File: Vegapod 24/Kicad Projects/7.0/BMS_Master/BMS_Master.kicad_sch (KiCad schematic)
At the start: 87 parts, among them IC1 B0505S-2W, J1 LV Battery, J2 ST-Link, J3 Conn_01x06_Pin, K1 ECK200BHAAEA, K2 ECK200BHAAEA, Q1 SI2318CDS (SI2318), Q2 SI2318CDS (SI2318), U1 KA78M12_TO252, U11 LM324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

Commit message: BMS Master completed
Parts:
- added C33: 100n, Capacitor_SMD:C_0805_2012Metric_Pad1.18x1.45mm_HandSolder, symbol Device:C_Small
- added C34, C35: 10uF, Capacitor_SMD:C_1206_3216Metric_Pad1.33x1.80mm_HandSolder, symbol Device:C_Small
- added J4: Batt Comm, Connector_PinSocket_2.00mm:PinSocket_1x05_P2.00mm_Vertical, symbol Connector:Conn_01x05_Pin
- added R32, R33, R34, R35, R36, R37: 470, Resistor_SMD:R_0805_2012Metric_Pad1.20x1.40mm_HandSolder, symbol Device:R_Small
- added U10, U14: 6N137, Package_SO:SSO-8_6.7x9.8mm_P2.54mm_Clearance8mm, symbol Isolator:6N137
- added U15: B0505S-1WR3, B0505S_MNS, symbol B0505-1WR3:B0505S-1WR3
- added U16: EL814, Package_DIP:SMDIP-4_W9.53mm_Clearance8mm, symbol Isolator:EL814
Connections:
- net +5VD: now also C33.2, C34.1, R34.2, U14.7 (EN), U14.8 (VCC), U15.2 (VIN)
- net GNDD: now also C33.1, C34.2, U10.3 (C), U14.5 (GND), U15.1 (GND), U16.2
- net RX: now also R34.1, U14.6 (VO)
- net TX: now also R33.2
- net PA8: now reaches U13.42 (PA8)
- net PA8: now also R37.2
- new net: J4.4 (Pin_4), R32.1, U10.6 (VO)
- new net: C35.1, J4.2 (Pin_2), R32.2, U10.7 (EN), U10.8 (VCC), U15.4 (+VO), U16.4
- new net: J4.5 (Pin_5), R36.1, U16.3
- new net: J4.3 (Pin_3), R35.1
- new net: R35.2, U14.2 (A)
- new net: R33.1, U10.2 (A)
- new net: R37.1, U16.1
- new net GND1: C35.2, J4.1 (Pin_1), R36.2, U10.5 (GND), U14.3 (C), U15.3 (0V)

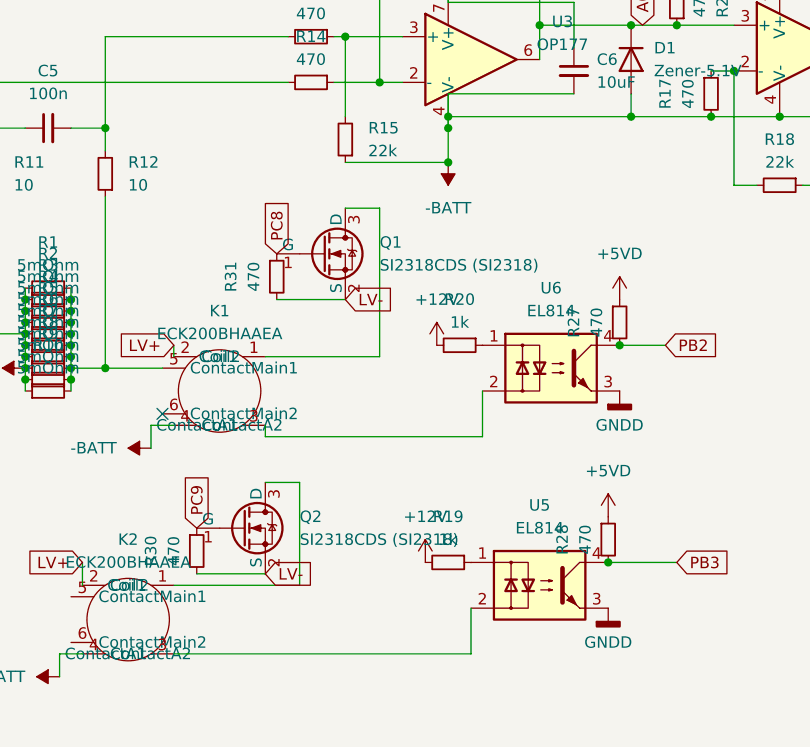
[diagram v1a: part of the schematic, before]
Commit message: Flyback diode for contactor
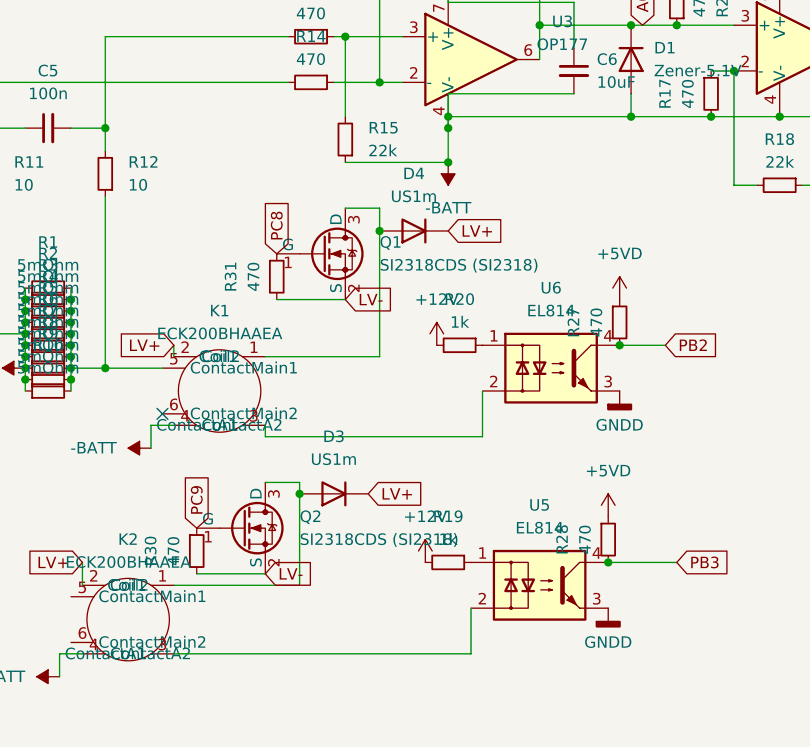
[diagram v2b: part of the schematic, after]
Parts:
- added D3, D4: US1m, Diode_SMD:D_SMA-SMB_Universal_Handsoldering, symbol Device:D
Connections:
- net LV+: now also D3.1 (K), D4.1 (K)
- net at K1.1 (Coil1), Q1.3 (D): now also D4.2 (A)
- net at K2.1 (Coil1), Q2.3 (D): now also D3.2 (A)
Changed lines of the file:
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@@
   (junction (at 214.63 86.36) (diameter 0) (color 0 0 0 0)
   )
+  (junction (at 78.74 111.76) (diameter 0) (color 0 0 0 0)
+  )
   (junction (at 482.6 78.74) (diameter 0) (color 0 0 0 0)
   )
@@
   (junction (at 50.8 50.8) (diameter 0) (color 0 0 0 0)
   )
+  (junction (at 87.63 82.55) (diameter 0) (color 0 0 0 0)
+  )
   (no_connect (at 63.5 102.87))
   (wire (pts (xy 367.03 52.07) (xy 358.14 52.07))
@@
     (stroke (width 0) (type default))
   )
-  (wire (pts (xy 87.63 80.01) (xy 87.63 96.52))
+  (wire (pts (xy 87.63 80.01) (xy 87.63 82.55))
     (stroke (width 0) (type default))
   )
@@
     (stroke (width 0) (type default))
   )
-  (wire (pts (xy 78.74 110.49) (xy 78.74 121.92))
+  (wire (pts (xy 78.74 110.49) (xy 78.74 111.76))
     (stroke (width 0) (type default))
   )
@@
     (stroke (width 0) (type default))
   )
+  (wire (pts (xy 78.74 111.76) (xy 78.74 121.92))
+    (stroke (width 0) (type default))
+  )
   (wire (pts (xy 245.11 92.71) (xy 260.35 92.71))
     (stroke (width 0) (type default))
@@
     (stroke (width 0) (type default))
   )
+  (wire (pts (xy 87.63 82.55) (xy 87.63 96.52))
+    (stroke (width 0) (type default))
+  )
   (wire (pts (xy 146.05 69.85) (xy 132.08 69.85))
     (stroke (width 0) (type default))
@@
     )
   )
+  (global_label "LV+" (shape input) (at 95.25 82.55 0) (fields_autoplaced)
+    (effects (font (size 1.27 1.27)) (justify left))
+    (property "Intersheetrefs" "${INTERSHEET_REFS}" (at 101.9243 82.55 0)
+      (effects (font (size 1.27 1.27)) (justify left) hide)
+    )
+  )
   (global_label "TX" (shape input) (at 358.14 90.17 180) (fields_autoplaced)
     (effects (font (size 1.27 1.27)) (justify right))
@@
     )
   )
+  (global_label "LV+" (shape input) (at 86.36 111.76 0) (fields_autoplaced)
+    (effects (font (size 1.27 1.27)) (justify left))
+    (property "Intersheetrefs" "${INTERSHEET_REFS}" (at 93.0343 111.76 0)
+      (effects (font (size 1.27 1.27)) (justify left) hide)
+    )
+  )
   (global_label "SWDIO" (shape input) (at 427.99 27.94 270) (fields_autoplaced)
     (effects (font (size 1.27 1.27)) (justify right))
@@
     )
   )
+  (symbol (lib_id "Device:D") (at 91.44 82.55 180) (unit 1)
+    (in_bom yes) (on_board yes) (dnp no) (fields_autoplaced)
+    (property "Reference" "D4" (at 91.44 76.2 0)
+      (effects (font (size 1.27 1.27)))
+    )
+    (property "Value" "US1m" (at 91.44 78.74 0)
+      (effects (font (size 1.27 1.27)))
+    )
+    (property "Footprint" "Diode_SMD:D_SMA-SMB_Universal_Handsoldering" (at 91.44 82.55 0)
+      (effects (font (size 1.27 1.27)) hide)
+    )
+    (property "Datasheet" "~" (at 91.44 82.55 0)
+      (effects (font (size 1.27 1.27)) hide)
+    )
+    (property "Sim.Device" "D" (at 91.44 82.55 0)
+      (effects (font (size 1.27 1.27)) hide)
+    )
+    (property "Sim.Pins" "1=K 2=A" (at 91.44 82.55 0)
+      (effects (font (size 1.27 1.27)) hide)
+    )
+    (pin "2")
+    (pin "1")
+    (instances
+      (project "BMS_Master"
+        (path "/932638ee-bc30-42e0-97cd-e4762c194981"
+          (reference "D4") (unit 1)
+        )
+      )
+    )
+  )
   (symbol (lib_id "Device:C_Small") (at 58.42 48.26 0) (unit 1)
     (in_bom yes) (on_board yes) (dnp no) (fields_autoplaced)
@@
         )
       )
+    )
+  )
+  (symbol (lib_id "Device:D") (at 82.55 111.76 180) (unit 1)
+    (in_bom yes) (on_board yes) (dnp no) (fields_autoplaced)
+    (property "Reference" "D3" (at 82.55 105.41 0)
+      (effects (font (size 1.27 1.27)))
+    )
+    (property "Value" "US1m" (at 82.55 107.95 0)
+      (effects (font (size 1.27 1.27)))
+    )
+    (property "Footprint" "Diode_SMD:D_SMA-SMB_Universal_Handsoldering" (at 82.55 111.76 0)
+      (effects (font (size 1.27 1.27)) hide)
+    )
+    (property "Datasheet" "~" (at 82.55 111.76 0)
+      (effects (font (size 1.27 1.27)) hide)
+    )
+    (property "Sim.Device" "D" (at 82.55 111.76 0)
+      (effects (font (size 1.27 1.27)) hide)
+    )
+    (property "Sim.Pins" "1=K 2=A" (at 82.55 111.76 0)
+      (effects (font (size 1.27 1.27)) hide)
+    )
+    (pin "2")
+    (pin "1")
+    (instances
+      (project "BMS_Master"
+        (path "/932638ee-bc30-42e0-97cd-e4762c194981"
+          (reference "D3") (unit 1)
+        )
+      )

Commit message: Add boot pin conn. (forgor💀)
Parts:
- added R59: SHORT OUT, Resistor_SMD:R_0402_1005Metric, symbol Device:R
- added R60: Open Circuit, Resistor_SMD:R_0402_1005Metric, symbol Device:R
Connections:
- net +3.3V: now also R60.2
- net GNDD: now also R59.1
- net at U13.61 (PB8): now also R59.2, R60.1
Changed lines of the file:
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@@
   (junction (at 102.87 22.86) (diameter 0) (color 0 0 0 0)
   )
+  (junction (at 405.13 120.65) (diameter 0) (color 0 0 0 0)
+  )
   (junction (at 53.34 91.44) (diameter 0) (color 0 0 0 0)
   )
@@
     (stroke (width 0) (type default))
   )
+  (wire (pts (xy 393.7 120.65) (xy 405.13 120.65))
+    (stroke (width 0) (type default))
+  )
   (wire (pts (xy 149.86 60.96) (xy 149.86 55.88))
     (stroke (width 0) (type default))
@@
     )
   )
+  (symbol (lib_id "power:GNDD") (at 405.13 128.27 0) (unit 1)
+    (in_bom yes) (on_board yes) (dnp no) (fields_autoplaced)
+    (property "Reference" "#PWR060" (at 405.13 134.62 0)
+      (effects (font (size 1.27 1.27)) hide)
+    )
+    (property "Value" "GNDD" (at 405.13 132.08 0)
+      (effects (font (size 1.27 1.27)))
+    )
+    (property "Footprint" "" (at 405.13 128.27 0)
+      (effects (font (size 1.27 1.27)) hide)
+    )
+    (property "Datasheet" "" (at 405.13 128.27 0)
+      (effects (font (size 1.27 1.27)) hide)
+    )
+    (pin "1")
+    (instances
+      (project "BMS_Master"
+        (path "/932638ee-bc30-42e0-97cd-e4762c194981"
+          (reference "#PWR060") (unit 1)
+        )
+      )
+    )
+  )
   (symbol (lib_id "power:+12V") (at 95.25 55.88 0) (unit 1)
     (in_bom yes) (on_board yes) (dnp no) (fields_autoplaced)
@@
     )
   )
+  (symbol (lib_id "Device:R") (at 405.13 116.84 180) (unit 1)
+    (in_bom yes) (on_board yes) (dnp no) (fields_autoplaced)
+    (property "Reference" "R60" (at 407.67 115.57 0)
+      (effects (font (size 1.27 1.27)) (justify right))
+    )
+    (property "Value" "Open Circuit" (at 407.67 118.11 0)
+      (effects (font (size 1.27 1.27)) (justify right))
+    )
+    (property "Footprint" "Resistor_SMD:R_0402_1005Metric" (at 406.908 116.84 90)
+      (effects (font (size 1.27 1.27)) hide)
+    )
+    (property "Datasheet" "~" (at 405.13 116.84 0)
+      (effects (font (size 1.27 1.27)) hide)
+    )
+    (pin "2")
+    (pin "1")
+    (instances
+      (project "LU"
+        (path "/735d61e3-154f-498a-961e-67a9bf0dff66"
+          (reference "R60") (unit 1)
+        )
+      )
+      (project "BMS_Master"
+        (path "/932638ee-bc30-42e0-97cd-e4762c194981"
+          (reference "R38") (unit 1)
+        )
+      )
+    )
+  )
   (symbol (lib_id "Device:C_Small") (at 135.89 33.02 0) (unit 1)
     (in_bom yes) (on_board yes) (dnp no) (fields_autoplaced)
@@
     )
   )
+  (symbol (lib_id "Device:R") (at 405.13 124.46 180) (unit 1)
+    (in_bom yes) (on_board yes) (dnp no) (fields_autoplaced)
+    (property "Reference" "R59" (at 407.67 123.19 0)
+      (effects (font (size 1.27 1.27)) (justify right))
+    )
+    (property "Value" "SHORT OUT" (at 407.67 125.73 0)
+      (effects (font (size 1.27 1.27)) (justify right))
+    )
+    (property "Footprint" "Resistor_SMD:R_0402_1005Metric" (at 406.908 124.46 90)
+      (effects (font (size 1.27 1.27)) hide)
+    )
+    (property "Datasheet" "~" (at 405.13 124.46 0)
+      (effects (font (size 1.27 1.27)) hide)
+    )
+    (pin "2")
+    (pin "1")
+    (instances
+      (project "LU"
+        (path "/735d61e3-154f-498a-961e-67a9bf0dff66"
+          (reference "R59") (unit 1)
+        )
+      )
+      (project "BMS_Master"
+        (path "/932638ee-bc30-42e0-97cd-e4762c194981"
+          (reference "R39") (unit 1)
+        )
+      )
+    )
+  )
   (symbol (lib_id "power:+3.3V") (at 186.69 20.32 0) (unit 1)
     (in_bom yes) (on_board yes) (dnp no) (fields_autoplaced)
@@
         )
       )
+    )
+  )
+  (symbol (lib_id "power:+3.3V") (at 405.13 113.03 0) (unit 1)
+    (in_bom yes) (on_board yes) (dnp no) (fields_autoplaced)
+    (property "Reference" "#PWR061" (at 405.13 116.84 0)
+      (effects (font (size 1.27 1.27)) hide)
+    )
+    (property "Value" "+3.3V" (at 405.13 107.95 0)
+      (effects (font (size 1.27 1.27)))
+    )
+    (property "Footprint" "" (at 405.13 113.03 0)
+      (effects (font (size 1.27 1.27)) hide)
+    )
+    (property "Datasheet" "" (at 405.13 113.03 0)
+      (effects (font (size 1.27 1.27)) hide)
+    )
+    (pin "1")
+    (instances
+      (project "BMS_Master"
+        (path "/932638ee-bc30-42e0-97cd-e4762c194981"
+          (reference "#PWR061") (unit 1)
+        )
+      )

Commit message: BMS Master changes because fucked up
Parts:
- added C36, C37: 10uF, Capacitor_SMD:C_1206_3216Metric_Pad1.33x1.80mm_HandSolder, symbol Device:C_Small
- added U17: B0505S-1WR3, B0505S_MNS, symbol B0505-1WR3:B0505S-1WR3
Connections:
- net +5V: now also C36.2, U17.2 (VIN)
- net -BATT: now also C36.1, C37.1, U17.1 (GND), U17.4 (+VO); no longer C11.2, C6.2, U3.4 (V-), U4.4 (V-)
- new net -5V: C11.2, C37.2, C6.2, U17.3 (0V), U3.4 (V-), U4.4 (V-)
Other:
- moved on the sheet: D2

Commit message: BMS Master final changes
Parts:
- added Q1 (x2): IRLZ44N, Package_TO_SOT_THT:TO-220-3_Vertical, symbol Transistor_FET:IRLZ44N
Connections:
- net GNDD: now also Q1.3 (S), Q1.3 (S)
- net PC8: now also Q1.1 (G)
- net PC9: now also Q1.1 (G)
- net at D4.2 (A), K1.1 (Coil1), Q1.3 (D): now also Q1.2 (D)
- net at D3.2 (A), K2.1 (Coil1), Q2.3 (D): now also Q1.2 (D)
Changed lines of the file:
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@@
   (junction (at 102.87 33.02) (diameter 0) (color 0 0 0 0)
   )
+  (junction (at 76.2 110.49) (diameter 0) (color 0 0 0 0)
+  )
   (junction (at 218.44 53.34) (diameter 0) (color 0 0 0 0)
   )
@@
   (junction (at 162.56 78.74) (diameter 0) (color 0 0 0 0)
   )
+  (junction (at 83.82 80.01) (diameter 0) (color 0 0 0 0)
+  )
   (junction (at 334.01 24.13) (diameter 0) (color 0 0 0 0)
   )
@@
     (stroke (width 0) (type default))
   )
+  (wire (pts (xy 55.88 106.68) (xy 55.88 109.22))
+    (stroke (width 0) (type default))
+  )
   (wire (pts (xy 172.72 50.8) (xy 172.72 53.34))
     (stroke (width 0) (type default))
@@
     (stroke (width 0) (type default))
   )
+  (wire (pts (xy 83.82 80.01) (xy 87.63 80.01))
+    (stroke (width 0) (type default))
+  )
   (wire (pts (xy 161.29 45.72) (xy 171.45 45.72))
     (stroke (width 0) (type default))
@@
     (stroke (width 0) (type default))
   )
+  (wire (pts (xy 81.28 68.58) (xy 81.28 80.01))
+    (stroke (width 0) (type default))
+  )
   (wire (pts (xy 466.09 101.6) (xy 467.36 101.6))
     (stroke (width 0) (type default))
@@
     (stroke (width 0) (type default))
   )
-  (wire (pts (xy 83.82 80.01) (xy 87.63 80.01))
+  (wire (pts (xy 81.28 80.01) (xy 83.82 80.01))
     (stroke (width 0) (type default))
   )
@@
     (stroke (width 0) (type default))
   )
+  (wire (pts (xy 76.2 110.49) (xy 78.74 110.49))
+    (stroke (width 0) (type default))
+  )
   (wire (pts (xy 115.57 59.69) (xy 105.41 59.69))
     (stroke (width 0) (type default))
@@
     (stroke (width 0) (type default))
   )
-  (wire (pts (xy 74.93 110.49) (xy 78.74 110.49))
+  (wire (pts (xy 74.93 110.49) (xy 76.2 110.49))
     (stroke (width 0) (type default))
   )
@@
     (stroke (width 0) (type default))
   )
+  (wire (pts (xy 55.88 109.22) (xy 76.2 109.22))
+    (stroke (width 0) (type default))
+  )
   (wire (pts (xy 214.63 81.28) (xy 233.68 81.28))
     (stroke (width 0) (type default))
@@
     (stroke (width 0) (type default))
   )
+  (wire (pts (xy 76.2 109.22) (xy 76.2 110.49))
+    (stroke (width 0) (type default))
+  )
   (wire (pts (xy 93.98 161.29) (xy 93.98 158.75))
     (stroke (width 0) (type default))
@@
     (stroke (width 0) (type default))
   )
+  (wire (pts (xy 46.99 106.68) (xy 55.88 106.68))
+    (stroke (width 0) (type default))
+  )
   (wire (pts (xy 127 59.69) (xy 120.65 59.69))
     (stroke (width 0) (type default))
@@
     (stroke (width 0) (type default))
   )
+  (wire (pts (xy 72.39 68.58) (xy 81.28 68.58))
+    (stroke (width 0) (type default))
+  )
   (wire (pts (xy 151.13 38.1) (xy 143.51 38.1))
     (stroke (width 0) (type default))
@@
     )
   )
+  (global_label "LV-" (shape input) (at 46.99 116.84 0) (fields_autoplaced)
+    (effects (font (size 1.27 1.27)) (justify left))
+    (property "Intersheetrefs" "${INTERSHEET_REFS}" (at 53.6643 116.84 0)
+      (effects (font (size 1.27 1.27)) (justify left) hide)
+    )
+  )
   (global_label "LV-" (shape input) (at 46.99 31.75 270) (fields_autoplaced)
     (effects (font (size 1.27 1.27)) (justify right))
@@
     )
   )
+  (global_label "PC9" (shape input) (at 39.37 111.76 180) (fields_autoplaced)
+    (effects (font (size 1.27 1.27)) (justify right))
+    (property "Intersheetrefs" "${INTERSHEET_REFS}" (at 32.6353 111.76 0)
+      (effects (font (size 1.27 1.27)) (justify right) hide)
+    )
+  )
   (global_label "LV-" (shape input) (at 217.17 86.36 270) (fields_autoplaced)
     (effects (font (size 1.27 1.27)) (justify right))
@@
     )
   )
+  (global_label "PC8" (shape input) (at 64.77 73.66 90) (fields_autoplaced)
+    (effects (font (size 1.27 1.27)) (justify left))
+    (property "Intersheetrefs" "${INTERSHEET_REFS}" (at 64.77 66.9253 90)
+      (effects (font (size 1.27 1.27)) (justify left) hide)
+    )
+  )
   (global_label "PB2" (shape input) (at 393.7 105.41 0) (fields_autoplaced)
     (effects (font (size 1.27 1.27)) (justify left))
@@
     )
   )
+  (global_label "LV-" (shape input) (at 72.39 78.74 270) (fields_autoplaced)
+    (effects (font (size 1.27 1.27)) (justify right))
+    (property "Intersheetrefs" "${INTERSHEET_REFS}" (at 72.39 85.4143 90)
+      (effects (font (size 1.27 1.27)) (justify right) hide)
+    )
+  )
   (global_label "CTRL" (shape input) (at 450.85 30.48 270) (fields_autoplaced)
     (effects (font (size 1.27 1.27)) (justify right))
@@
     )
   )
+  (symbol (lib_id "Transistor_FET:IRLZ44N") (at 69.85 73.66 0) (unit 1)
+    (in_bom yes) (on_board yes) (dnp no) (fields_autoplaced)
+    (property "Reference" "Q1" (at 76.2 72.39 0)
+      (effects (font (size 1.27 1.27)) (justify left))
+    )
+    (property "Value" "IRLZ44N" (at 76.2 74.93 0)
+      (effects (font (size 1.27 1.27)) (justify left))
+    )
+    (property "Footprint" "Package_TO_SOT_THT:TO-220-3_Vertical" (at 76.2 75.565 0)
+      (effects (font (size 1.27 1.27) italic) (justify left) hide)
+    )
+    (property "Datasheet" "http://www.irf.com/product-info/datasheets/data/irlz44n.pdf" (at 69.85 73.66 0)
+      (effects (font (size 1.27 1.27)) (justify left) hide)
+    )
+    (pin "2")
+    (pin "1")
+    (pin "3")
+    (instances
+      (project "Chg_Dschg Controller"
+        (path "/44b4c7bd-7876-4094-a297-c391da939751"
+          (reference "Q1") (unit 1)
+        )
+      )
+      (project "BMS_Master"
+        (path "/932638ee-bc30-42e0-97cd-e4762c194981"
+          (reference "Q3") (unit 1)
+        )
+      )
+    )
+  )
   (symbol (lib_id "Isolator:EL814") (at 106.68 97.79 0) (unit 1)
     (in_bom yes) (on_board yes) (dnp no) (fields_autoplaced)
@@
         )
       )
+    )
+  )
+  (symbol (lib_id "Transistor_FET:IRLZ44N") (at 44.45 111.76 0) (unit 1)
+    (in_bom yes) (on_board yes) (dnp no) (fields_autoplaced)
+    (property "Reference" "Q1" (at 50.8 110.49 0)
+      (effects (font (size 1.27 1.27)) (justify left))
+    )
+    (property "Value" "IRLZ44N" (at 50.8 113.03 0)
+      (effects (font (size 1.27 1.27)) (justify left))
+    )
+    (property "Footprint" "Package_TO_SOT_THT:TO-220-3_Vertical" (at 50.8 113.665 0)
+      (effects (font (size 1.27 1.27) italic) (justify left) hide)
+    )
+    (property "Datasheet" "http://www.irf.com/product-info/datasheets/data/irlz44n.pdf" (at 44.45 111.76 0)
+      (effects (font (size 1.27 1.27)) (justify left) hide)
+    )
+    (pin "2")
+    (pin "1")
+    (pin "3")
+    (instances
+      (project "Chg_Dschg Controller"
+        (path "/44b4c7bd-7876-4094-a297-c391da939751"
+          (reference "Q1") (unit 1)
+        )
+      )
+      (project "BMS_Master"
+        (path "/932638ee-bc30-42e0-97cd-e4762c194981"
+          (reference "Q4") (unit 1)
+        )
+      )
